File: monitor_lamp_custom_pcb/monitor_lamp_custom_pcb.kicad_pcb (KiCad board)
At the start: 4 copper layers, 50 x 35 mm, 33 parts, among them IC1 HUSB238, J1 USB_C_Receptacle_PowerOnly_6P, J2 VEML7700_Connection, J3 LD2410C_Connection, J4 Conn_01x02, Q1 AO3401A, Q3 AO3400A, U1 TPS563300, U2 TPS561208DDCT, U3 ESP32-C3_SUPERMINI_TH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

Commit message: Tracing some routes
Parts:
- moved R6 1.31 mm to (137.1, 77.8), turned to 180 degrees
- moved Q3 0.40 mm to (140.9, 77.8)
- moved D1 0.35 mm to (140.8, 81.8)
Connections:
- J2 pad 1: /ESP32_Sensors_Mosfet/+5V -> /ESP32_Sensors_Mosfet/5V_Protected
- J3 pad 1: /ESP32_Sensors_Mosfet/+5V -> /ESP32_Sensors_Mosfet/5V_Protected
- U3 pad 5V: Net-(U4-OUT) -> /ESP32_Sensors_Mosfet/5V_Protected
- U4 pad 5: Net-(U4-OUT) -> /ESP32_Sensors_Mosfet/5V_Protected
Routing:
- net /ESP32_Sensors_Mosfet/5V_Protected: track 0.00 -> 23.5 mm
- added copper zone on F.Cu, net /+12V
- added copper zone on B.Cu, net GND
- removed copper zone on In1.Cu, net GND
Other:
- copper layers 4 -> 2
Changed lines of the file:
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@@
 	(layers
 		(0 "F.Cu" signal)
-		(4 "In1.Cu" signal)
-		(6 "In2.Cu" signal)
 		(2 "B.Cu" signal)
 		(9 "F.Adhes" user "F.Adhesive")
@@
 			)
 			(layer "dielectric 1"
-				(type "prepreg")
-				(thickness 0.1)
-				(material "FR4")
-				(epsilon_r 4.5)
-				(loss_tangent 0.02)
-			)
-			(layer "In1.Cu"
-				(type "copper")
-				(thickness 0.035)
-			)
-			(layer "dielectric 2"
 				(type "core")
-				(thickness 1.24)
-				(material "FR4")
-				(epsilon_r 4.5)
-				(loss_tangent 0.02)
-			)
-			(layer "In2.Cu"
-				(type "copper")
-				(thickness 0.035)
-			)
-			(layer "dielectric 3"
-				(type "prepreg")
-				(thickness 0.1)
+				(thickness 1.51)
 				(material "FR4")
 				(epsilon_r 4.5)
@@
 			(layers "*.Cu" "*.Mask")
 			(remove_unused_layers no)
-			(net "Net-(U4-OUT)")
+			(net "/ESP32_Sensors_Mosfet/5V_Protected")
 			(pinfunction "5V_5V")
 			(pintype "power_in")
@@
 			(layers "F.Cu" "F.Mask" "F.Paste")
 			(roundrect_rratio 0.25)
-			(net "Net-(U4-OUT)")
+			(net "/ESP32_Sensors_Mosfet/5V_Protected")
 			(pinfunction "OUT_5")
 			(pintype "passive")
@@
 			(layers "F.Cu" "F.Mask" "F.Paste")
 			(roundrect_rratio 0.25)
-			(net "/ESP32_Sensors_Mosfet/+5V")
+			(net "/ESP32_Sensors_Mosfet/5V_Protected")
 			(pinfunction "Pin_1_1")
 			(pintype "passive")
@@
 	(footprint "Resistor_SMD:R_0603_1608Metric"
 		(layer "F.Cu")
-		(at 137.9025 78.76 -90)
+		(at 137.075 77.75 180)
 		(descr "Resistor SMD 0603 (1608 Metric), square (rectangular) end terminal, IPC-7351 nominal, (Body size source: IPC-SM-782 page 72, https://www.pcb-3d.com/wordpress/wp-content/uploads/ipc-sm-782a_amendment_1_and_2.pdf)")
 		(tags "resistor")
 		(property "Reference" "R6"
-			(at 0 -1.43 90)
+			(at 0 -1.43 0)
 			(layer "F.SilkS")
 			(effects
@@
 		)
 		(property "Value" "100k"
-			(at 0 1.43 90)
+			(at 0 1.43 0)
 			(layer "F.Fab")
 			(effects
@@
 		)
 		(property "Datasheet" ""
-			(at 0 0 90)
+			(at 0 0 0)
 			(layer "F.Fab")
 			(hide yes)
@@
 		)
 		(property "Description" "Resistor"
-			(at 0 0 90)
+			(at 0 0 0)
 			(layer "F.Fab")
 			(hide yes)
@@
 		)
 		(property "KiLib_Generator" "SMD_2terminal_chip_molded"
-			(at 0 0 90)
+			(at 0 0 0)
 			(layer "F.SilkS")
 			(hide yes)
@@
 		)
 		(fp_text user "${REFERENCE}"
-			(at 0 0 90)
+			(at 0 0 0)
 			(layer "F.Fab")
 			(effects
@@
 		)
 		(pad "1" smd roundrect
-			(at -0.825 0 270)
+			(at -0.825 0 180)
 			(size 0.8 0.95)
 			(layers "F.Cu" "F.Mask" "F.Paste")
@@
 		)
 		(pad "2" smd roundrect
-			(at 0.825 0 270)
+			(at 0.825 0 180)
 			(size 0.8 0.95)
 			(layers "F.Cu" "F.Mask" "F.Paste")
@@
 	(footprint "Package_TO_SOT_SMD:SOT-23"
 		(layer "F.Cu")
-		(at 141.34 77.81)
+		(at 140.9375 77.8)
 		(descr "SOT, 3 Pin (JEDEC TO-236 Var AB https://www.jedec.org/document_search?search_api_views_fulltext=TO-236)")
 		(tags "SOT TO_SOT_SMD")
@@
 	(footprint "Diode_SMD:D_SOD-323"
 		(layer "F.Cu")
-		(at 140.5 81.5 90)
+		(at 140.75 81.75 90)
 		(descr "SOD-323")
 		(tags "SOD-323")
@@
 			(layers "F.Cu" "F.Mask" "F.Paste")
 			(roundrect_rratio 0.25)
-			(net "/ESP32_Sensors_Mosfet/+5V")
+			(net "/ESP32_Sensors_Mosfet/5V_Protected")
 			(pinfunction "Pin_1_1")
 			(pintype "passive")
@@
 		(net "PWM_Control")
 	)
+	(segment
+		(start 156.74 55.6)
+		(end 157.5 54.84)
+		(width 0.2)
+		(layer "F.Cu")
+		(net "/ESP32_Sensors_Mosfet/5V_Protected")
+	)
+	(segment
+		(start 160.25 64.75)
+		(end 160.5 65)
+		(width 0.2)
+		(layer "F.Cu")
+		(net "/ESP32_Sensors_Mosfet/5V_Protected")
+	)
+	(segment
+		(start 163.25 59.75)
+		(end 160.25 62.75)
+		(width 0.2)
+		(layer "F.Cu")
+		(net "/ESP32_Sensors_Mosfet/5V_Protected")
+	)
+	(segment
+		(start 162.95 56.7)
+		(end 163.25 57)
+		(width 0.2)
+		(layer "F.Cu")
+		(net "/ESP32_Sensors_Mosfet/5V_Protected")
+	)
+	(segment
+		(start 160.25 62.75)
+		(end 160.25 64.75)
+		(width 0.2)
+		(layer "F.Cu")
+		(net "/ESP32_Sensors_Mosfet/5V_Protected")
+	)
+	(segment
+		(start 157.14 56)
+		(end 156.74 55.6)
+		(width 0.2)
+		(layer "F.Cu")
+		(net "/ESP32_Sensors_Mosfet/5V_Protected")
+	)
+	(segment
+		(start 161.5 56.7)
+		(end 160.8 56)
+		(width 0.2)
+		(layer "F.Cu")
+		(net "/ESP32_Sensors_Mosfet/5V_Protected")
+	)
+	(segment
+		(start 160.5 65)
+		(end 161.5 65)
+		(width 0.2)
+		(layer "F.Cu")
+		(net "/ESP32_Sensors_Mosfet/5V_Protected")
+	)
+	(segment
+		(start 151.775 55.6)
+		(end 156.74 55.6)
+		(width 0.3)
+		(layer "F.Cu")
+		(net "/ESP32_Sensors_Mosfet/5V_Protected")
+	)
+	(segment
+		(start 160.8 56)
+		(end 157.14 56)
+		(width 0.2)
+		(layer "F.Cu")
+		(net "/ESP32_Sensors_Mosfet/5V_Protected")
+	)
+	(segment
+		(start 163.25 57)
+		(end 163.25 59.75)
+		(width 0.2)
+		(layer "F.Cu")
+		(net "/ESP32_Sensors_Mosfet/5V_Protected")
+	)
+	(segment
+		(start 161.5 56.7)
+		(end 162.95 56.7)
+		(width 0.2)
+		(layer "F.Cu")
+		(net "/ESP32_Sensors_Mosfet/5V_Protected")
+	)
+	(zone
+		(net "/+12V")
+		(layer "F.Cu")
+		(hatch edge 0.5)
+		(priority 1)
+		(connect_pads yes
+			(clearance 0.5)
+		)
+		(min_thickness 0.25)
+		(fill yes
+			(thermal_gap 0.5)
+			(thermal_bridge_width 0.5)
+			(island_removal_mode 0)
+		)
+		(polygon
+			(pts
+				(xy 128.75 78.5) (xy 128.75 81.75) (xy 132 81.75) (xy 133.75 81.75) (xy 133.75 82.5) (xy 136.250077 82.5)
+				(xy 138.248527 84.499063) (xy 146.999913 84.500628) (xy 147 82.511291) (xy 139.761545 82.48794)
+				(xy 137.546844 80.261427) (xy 133.25 80.25) (xy 131.888889 78.5)
+			)
+		)
+	)
 	(zone
 		(net "GND")
-		(layer "In1.Cu")
-		(name "GND")
+		(layer "B.Cu")
 		(hatch edge 0.5)
 		(connect_pads
@@
 		)
 		(min_thickness 0.25)
-		(fill
+		(fill yes
 			(thermal_gap 0.5)
 			(thermal_bridge_width 0.5)
@@
 		(polygon
 			(pts
-				(xy 166.5 53) (xy 115.5 53) (xy 115.5 88.5) (xy 166.5 88.5)
+				(xy 166 53) (xy 115.75 53) (xy 115.75 88.5) (xy 166.25 88.5)
 			)
 		)

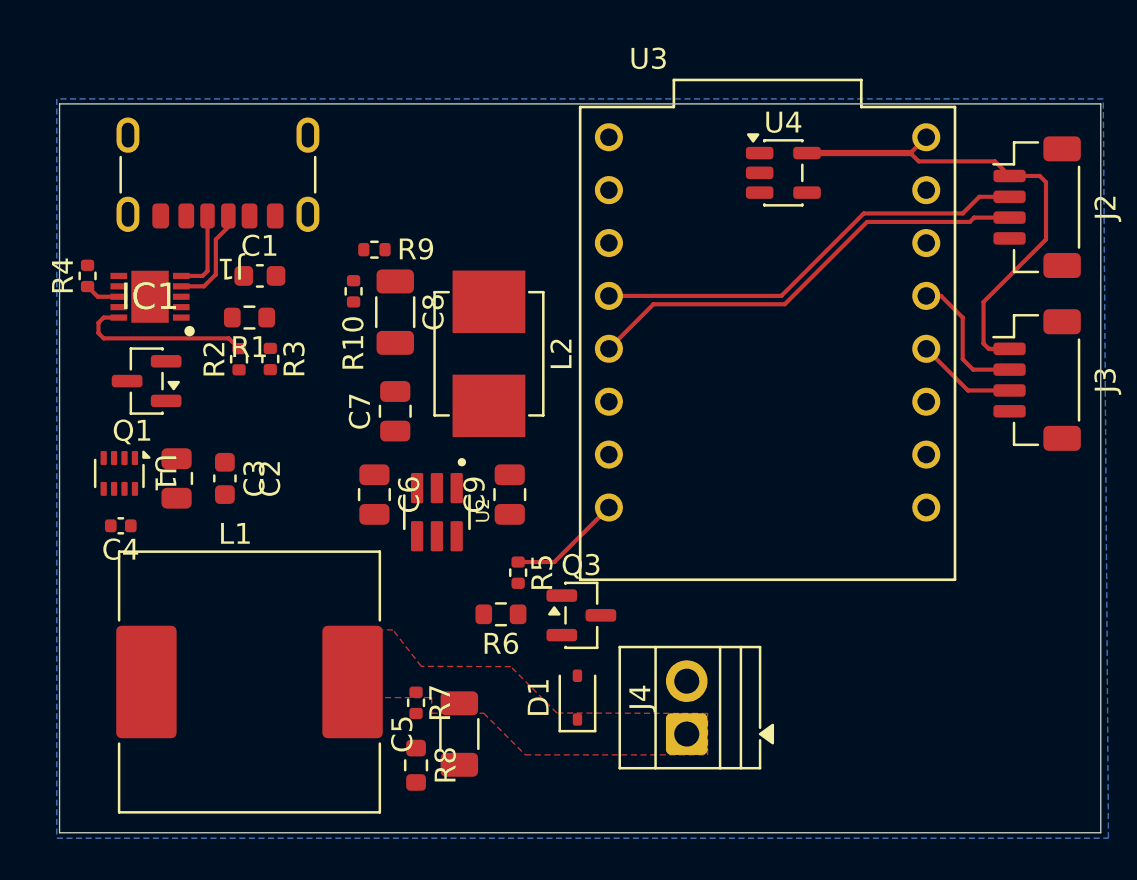
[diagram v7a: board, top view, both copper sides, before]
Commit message: Trace all routes and zone on pcb
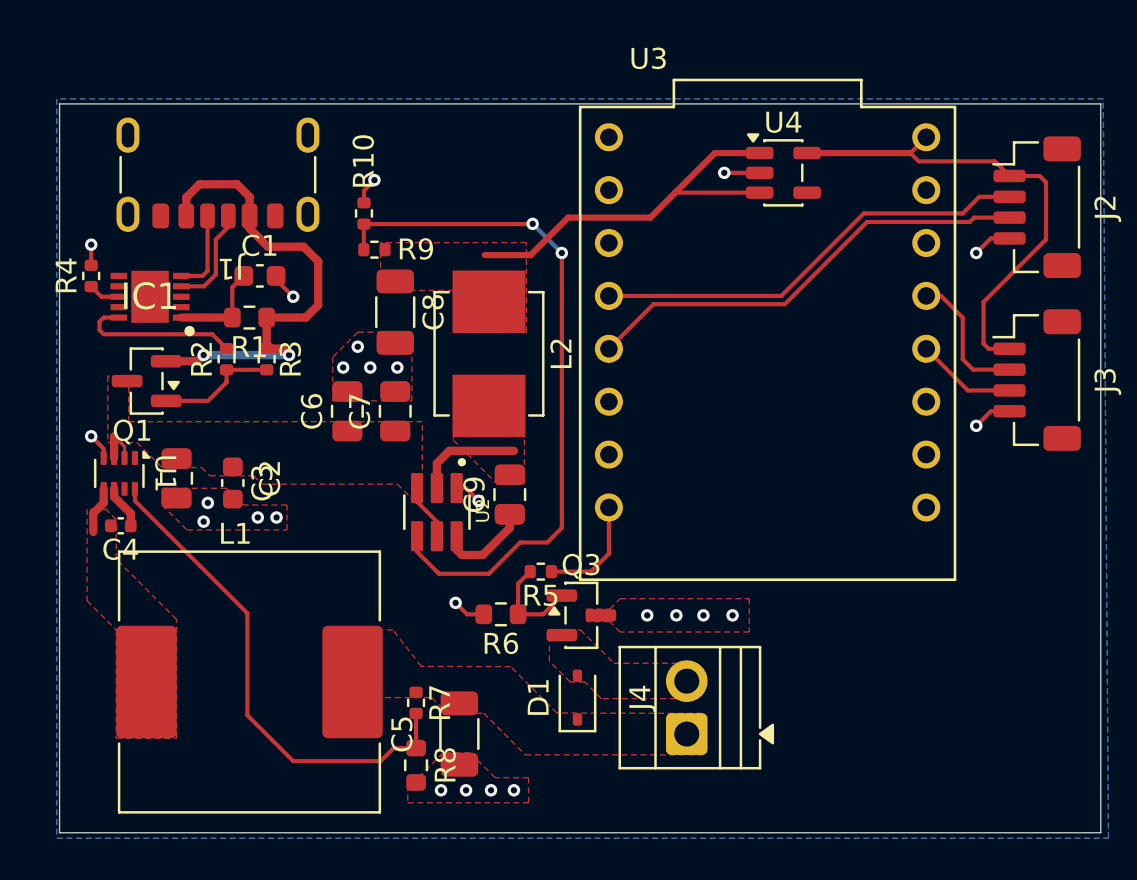
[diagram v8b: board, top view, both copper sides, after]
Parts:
- moved C6 4.21 mm to (129.7, 68.0), turned to 90 degrees
- moved R10 3.77 mm to (130.5, 58.5), turned to 90 degrees
- moved R5 1.09 mm to (139.0, 75.7), turned to 180 degrees
- moved R2 0.60 mm to (123.9, 65.5)
- moved C3 0.44 mm to (124.2, 71.4)
- moved R3 0.18 mm to (125.8, 65.5)
- moved R4 0.18 mm to (117.4, 61.5)
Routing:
- net Net-(U2-VFB): track 0.00 -> 33.6 mm, vias 0 -> 2
- net Net-(U1-FB): track 0.00 -> 24.0 mm
- net Net-(Q1-S): track 0.00 -> 23.4 mm, vias 0 -> 2
- net /+5V: track 0.00 -> 19.3 mm
- net GND: track 0.00 -> 13.3 mm, vias 0 -> 25
- net Net-(Q1-G): track 0.00 -> 5.79 mm
- net Net-(U2-SW): track 0.00 -> 5.14 mm
- net /+15V: track 0.00 -> 5.00 mm
- net Net-(Q3-G): track 0.00 -> 4.78 mm
- net Net-(IC1-VIN): track 0.00 -> 4.68 mm
- net Net-(U2-VBST): track 0.00 -> 4.49 mm
- net Net-(U1-SW): track 0.00 -> 2.28 mm
- net Net-(U1-BST): track 0.00 -> 2.11 mm
- net Net-(IC1-GATE): track 8.64 -> 7.88 mm
- added copper zone on F.Cu, net /+15V
- added copper zone on F.Cu, net /+5V
- added copper zone on F.Cu, net GND
- added copper zone on F.Cu, net Net-(D1-A)
- added copper zone on F.Cu, net Net-(U1-SW)
- added copper zone on F.Cu, net Net-(U2-SW)
